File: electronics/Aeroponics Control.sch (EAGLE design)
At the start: 27 parts, among them IC1 7407N, K1 SRM-1C-SL-5VDC, Q1 FQP30N06L, Q2 FQP30N06L, Q6 FDU3N40TU

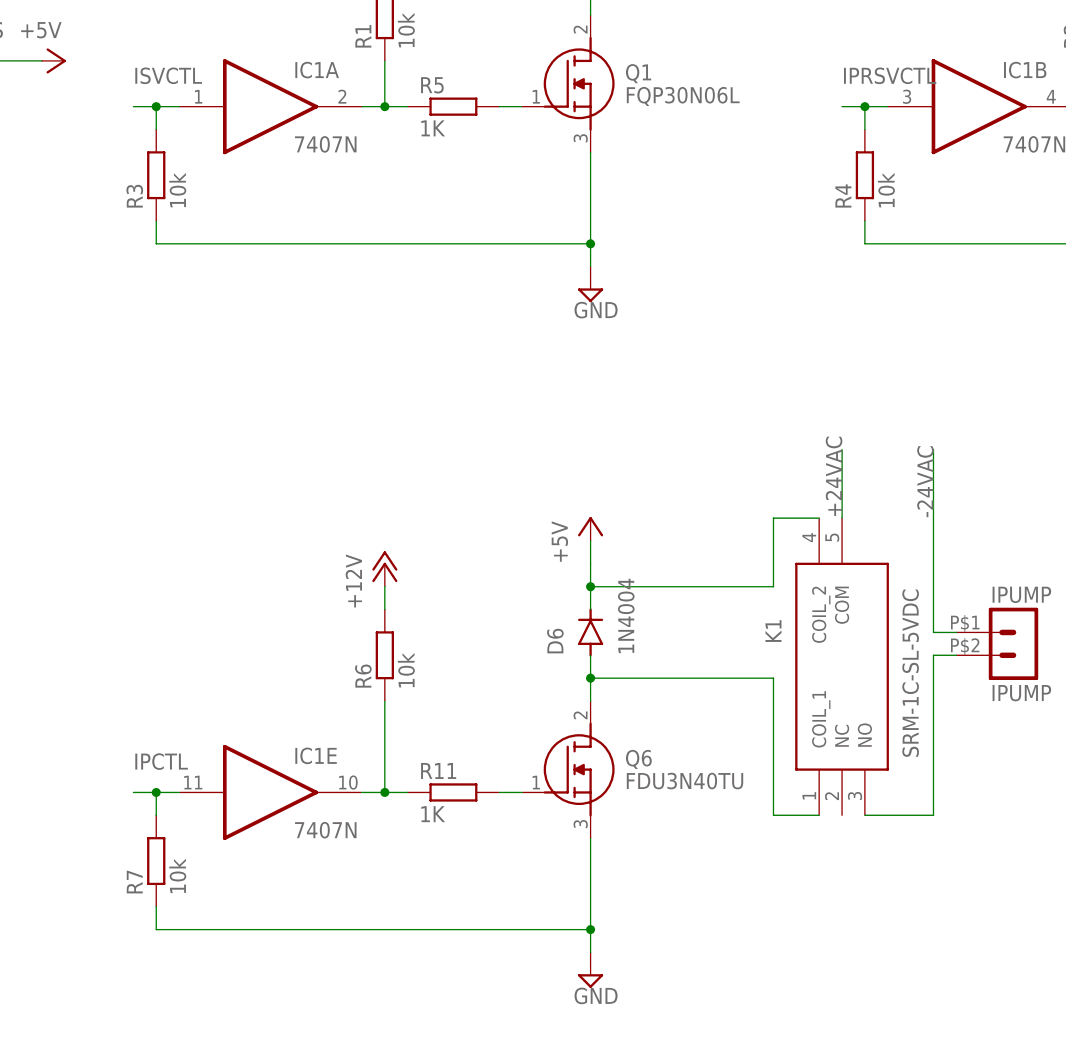
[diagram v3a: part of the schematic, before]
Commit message: 8695xzbdw: Fix for flush valve opening on microcontroller reset
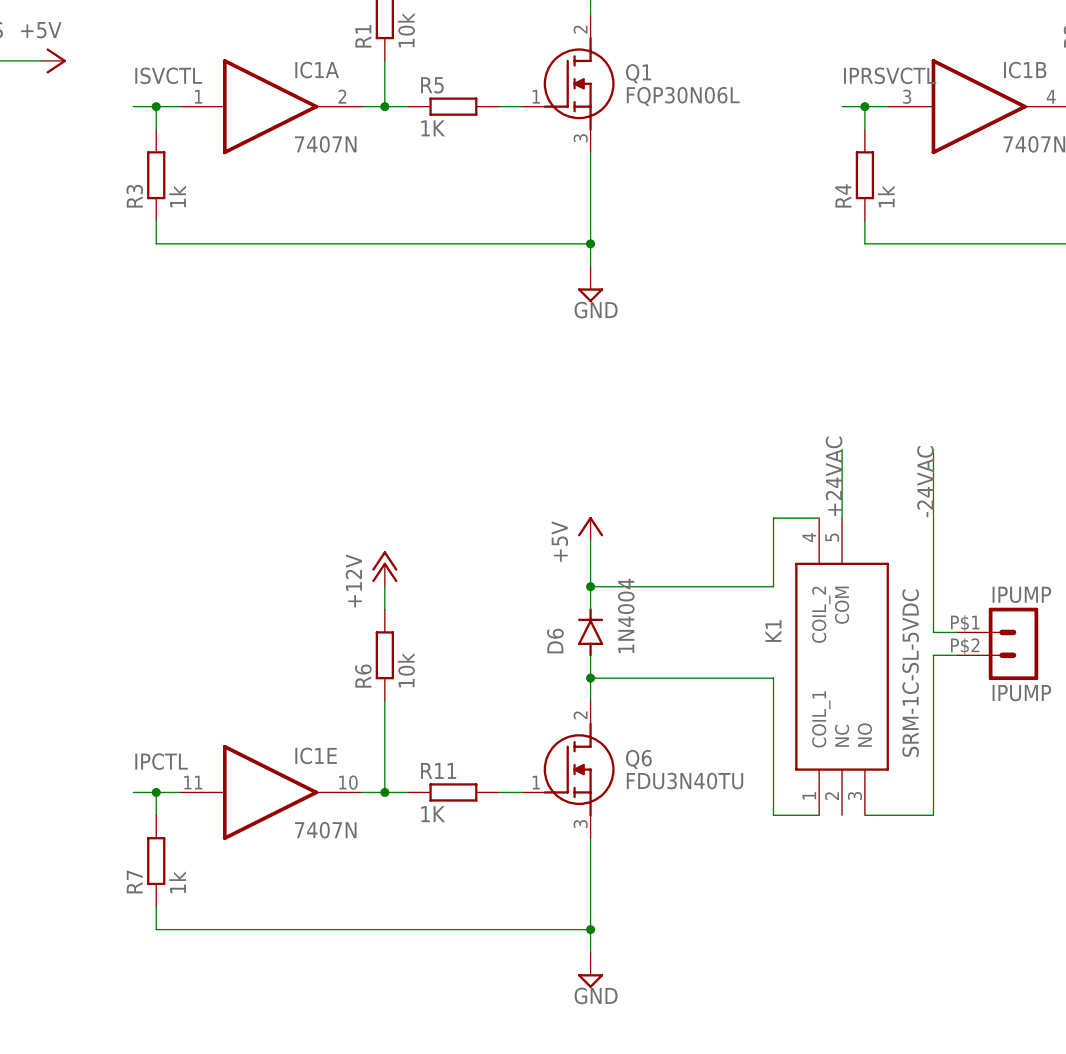
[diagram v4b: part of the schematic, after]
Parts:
- R3, R4, R7: value 10k -> 1k
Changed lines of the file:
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@@
 <part name="P+19" library="Aeroponics Control" deviceset="+12V" device=""/>
 <part name="SUPPLY7" library="Aeroponics Control" deviceset="GND" device=""/>
-<part name="R3" library="Aeroponics Control" deviceset="R-EU_" device="0204/7" package3d_urn="urn:adsk.eagle:package:23498/2" value="10k"/>
-<part name="R4" library="Aeroponics Control" deviceset="R-EU_" device="0204/7" package3d_urn="urn:adsk.eagle:package:23498/2" value="10k"/>
-<part name="R7" library="Aeroponics Control" deviceset="R-EU_" device="0204/7" package3d_urn="urn:adsk.eagle:package:23498/2" value="10k"/>
+<part name="R3" library="Aeroponics Control" deviceset="R-EU_" device="0204/7" package3d_urn="urn:adsk.eagle:package:23498/2" value="1k"/>
+<part name="R4" library="Aeroponics Control" deviceset="R-EU_" device="0204/7" package3d_urn="urn:adsk.eagle:package:23498/2" value="1k"/>
+<part name="R7" library="Aeroponics Control" deviceset="R-EU_" device="0204/7" package3d_urn="urn:adsk.eagle:package:23498/2" value="1k"/>
 </parts>
 <sheets>

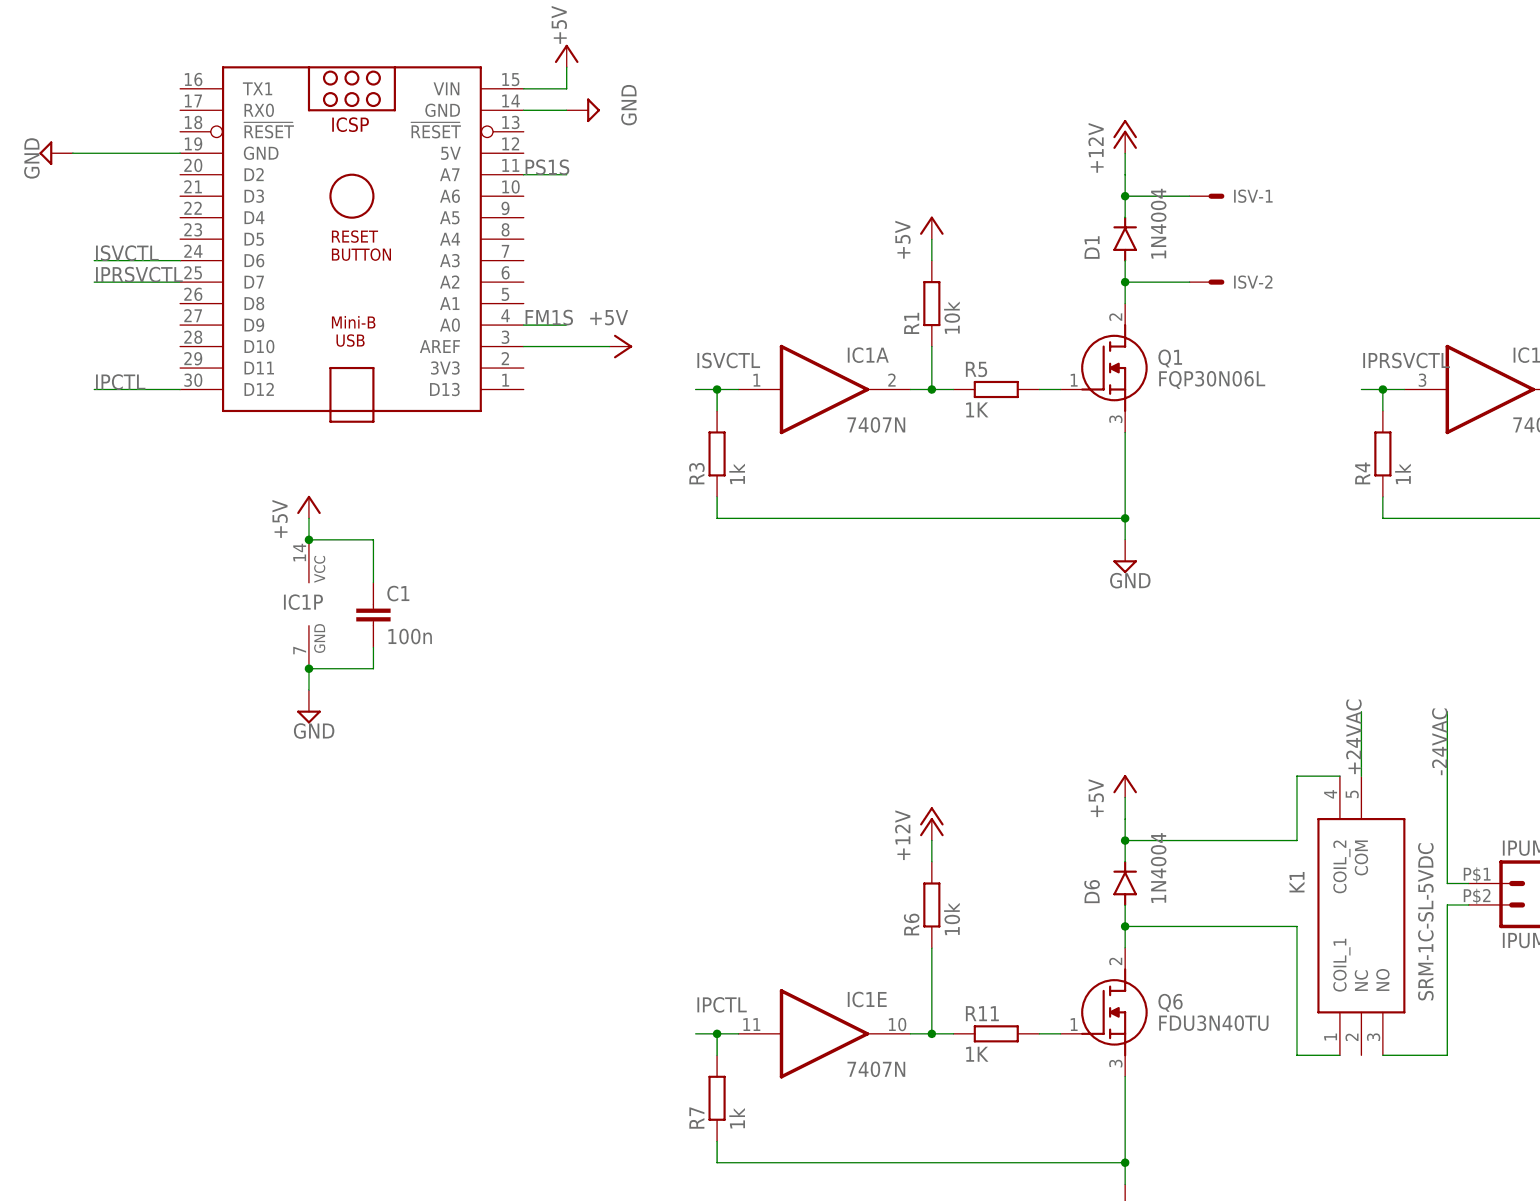
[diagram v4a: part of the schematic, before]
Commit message: Fixed FMS1 pin assignment on Nano. Incorpated fixed Relay library component.
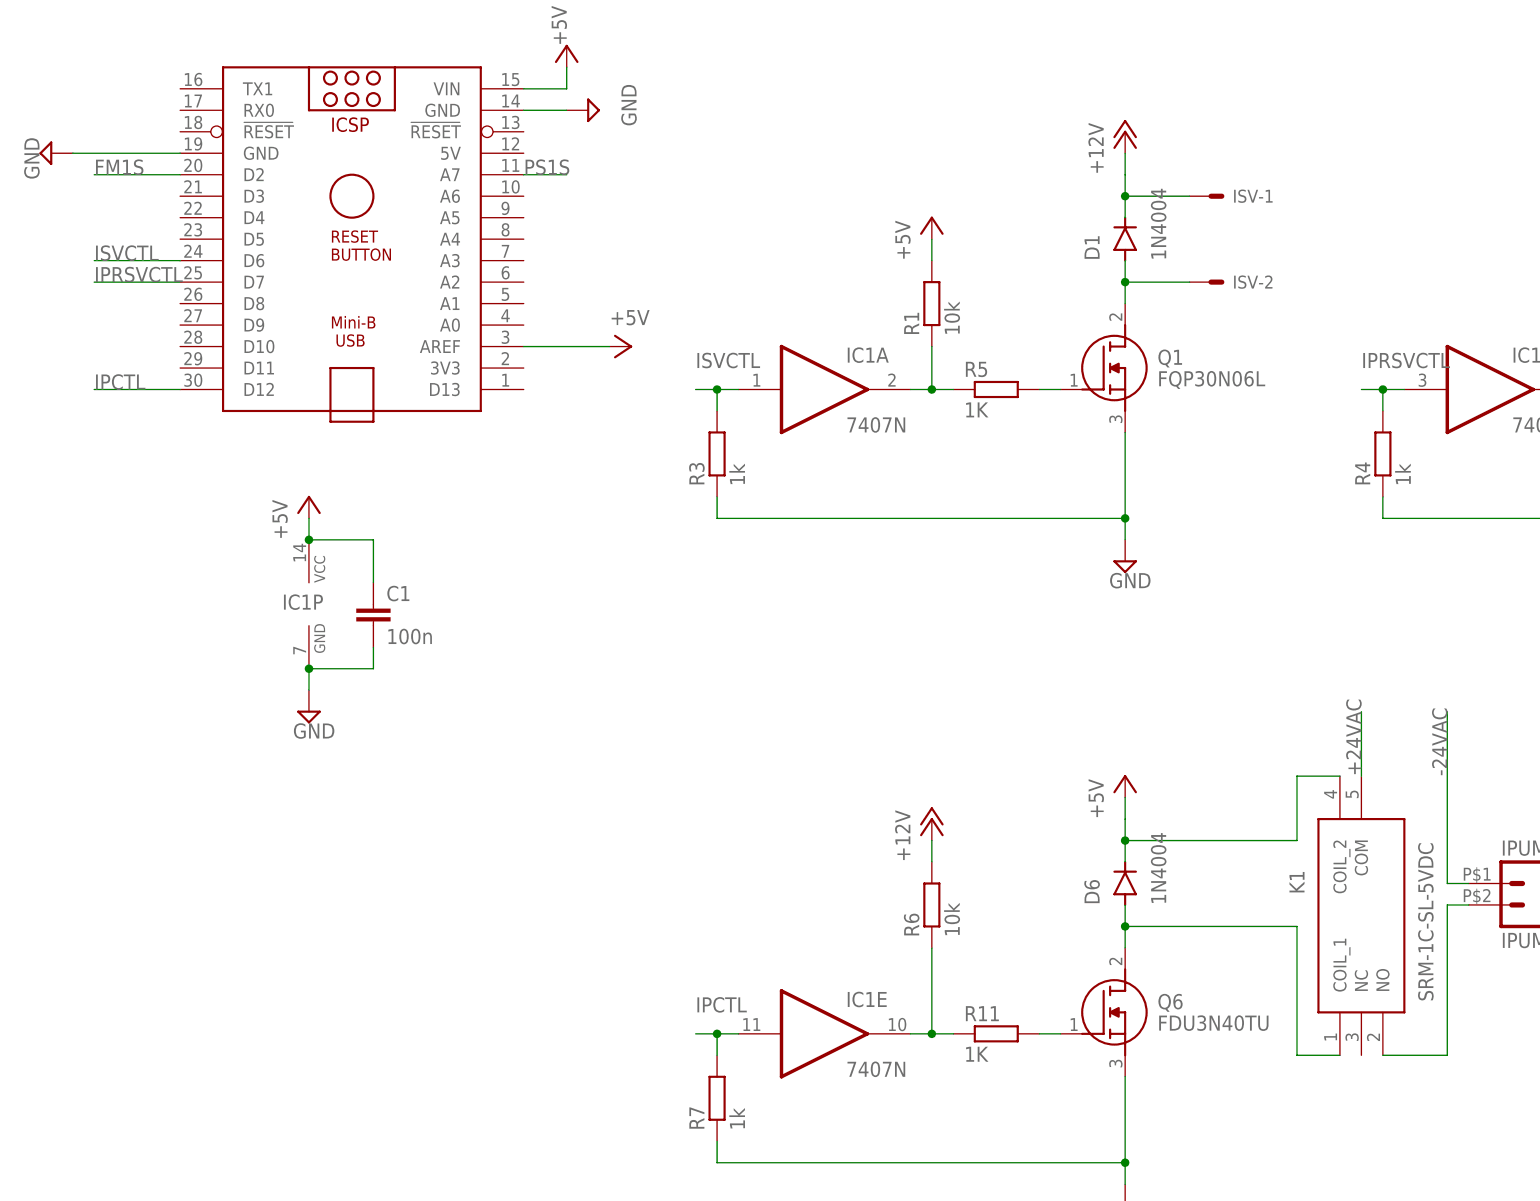
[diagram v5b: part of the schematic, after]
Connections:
- net FM1S: now also PCB1.D2; no longer PCB1.A0
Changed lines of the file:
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@@
 </instance>
 <instance part="P+14" gate="1" x="45.72" y="38.1" smashed="yes" rot="R270">
-<attribute name="VALUE" x="40.64" y="40.64" size="1.778" layer="96"/>
+<attribute name="VALUE" x="43.18" y="40.64" size="1.778" layer="96"/>
 </instance>
 <instance part="C1" gate="G$1" x="15.24" y="7.62" smashed="yes">
@@
 </segment>
 <segment>
-<pinref part="PCB1" gate="G$1" pin="A0"/>
-<wire x1="33.02" y1="40.64" x2="38.1" y2="40.64" width="0.1524" layer="91"/>
-<label x="33.02" y="40.64" size="1.778" layer="95"/>
-</segment>
-</net>
+<pinref part="PCB1" gate="G$1" pin="D2"/>
+<wire x1="-7.62" y1="58.42" x2="-17.78" y2="58.42" width="0.1524" layer="91"/>
+<label x="-17.78" y="58.42" size="1.778" layer="95"/>
+</segment>
+</net>
